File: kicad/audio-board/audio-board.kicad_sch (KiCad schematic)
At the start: 30 parts, among them U1 ADAU1861, U2 ADXL354CEZ, U3 LTC6242, U4 IM72D128VV01, U5 AD2428WBCPZ

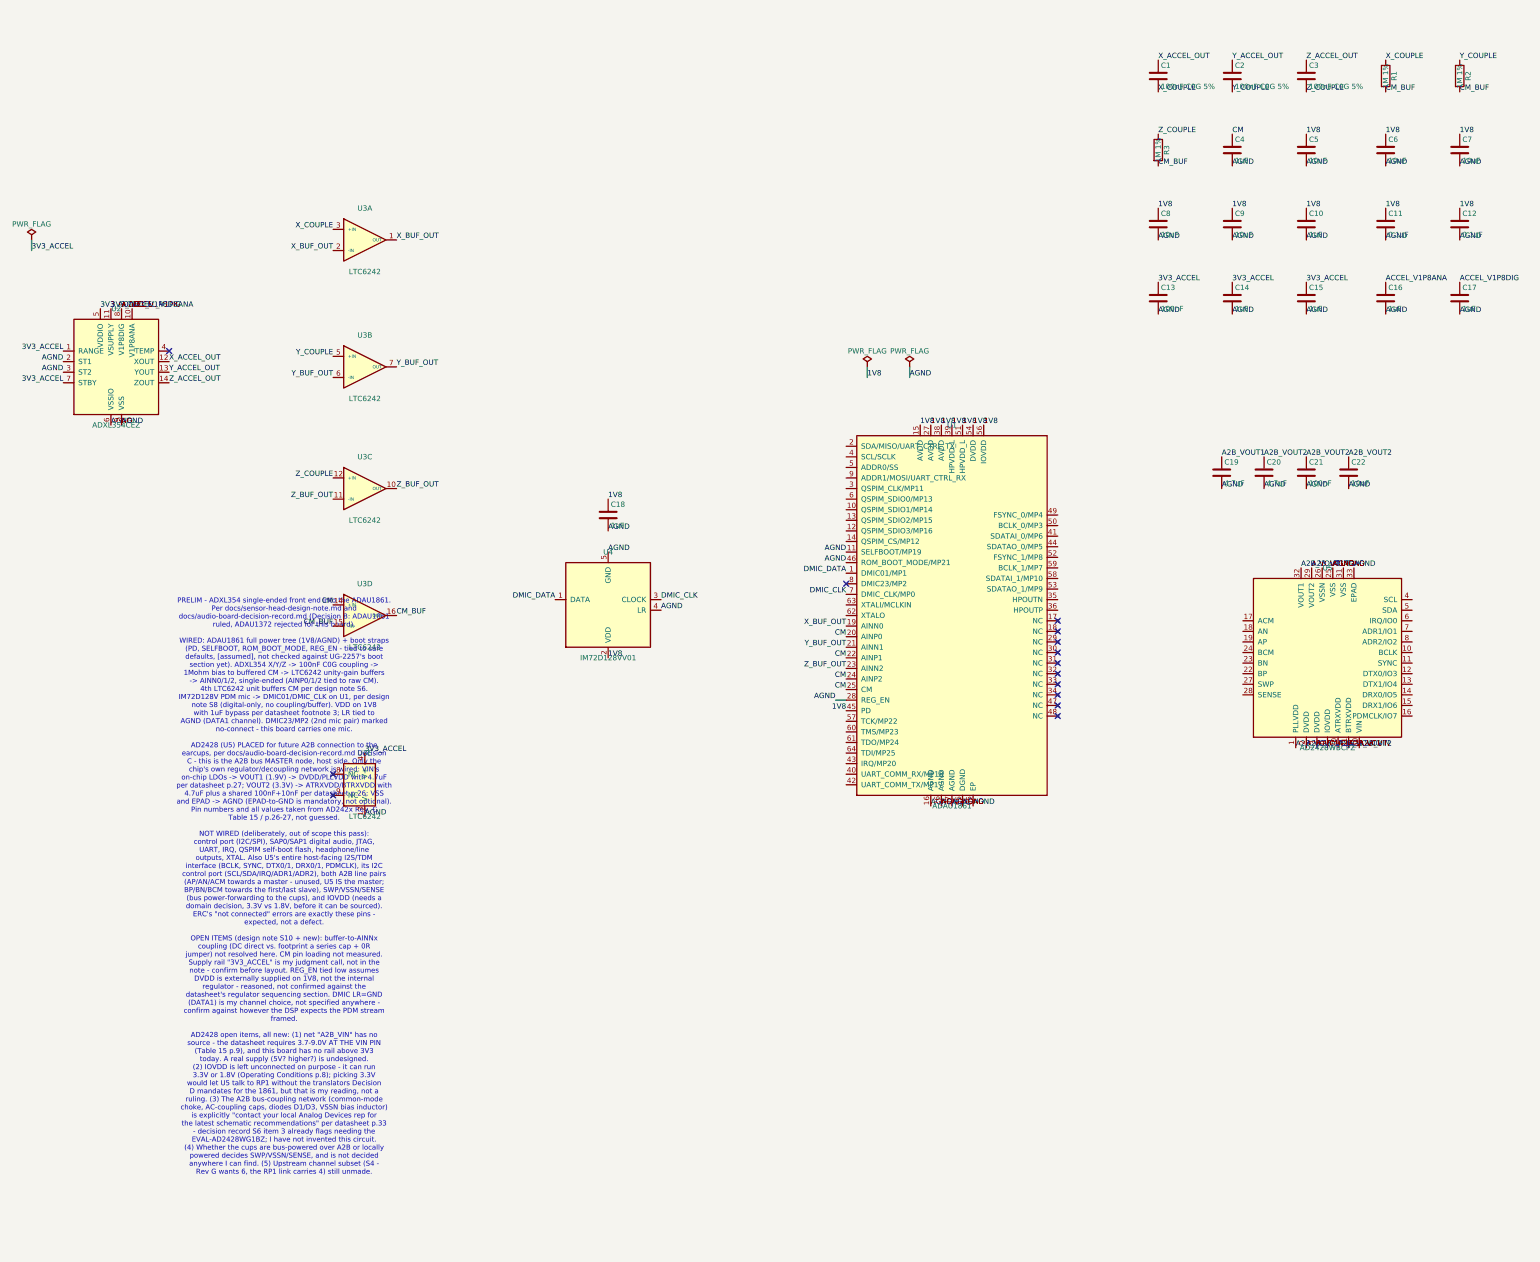
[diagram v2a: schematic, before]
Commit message: [LIMA] cross U1's I2S and I2C to the 3.3V host (CM5/RP1), per docs/audio-board-level-shifter.md
Two SN74LVC8T245 (U6 up, U7 down) carry the five ruled lines - BCLK_0, FSYNC_0, SDATAO_0,
SDATAO_1 up (DIR=1V8), SDATAI_0 down (DIR=AGND) - both parts tied OE=AGND (enabled). Same part on
both per the doc's own "route through the same device type so delays track" rule; U7 is oversized
for its one line on purpose. BCLK_1<-BCLK_0 and FSYNC_1<-FSYNC_0 are wired locally on U1 (no
translator) per the doc's S3.1, keeping SPT0/SPT1 sample-aligned across the two ports carrying the
3-mic array - closes the exact silent-failure mode that section calls out. SDATAI_1 is genuinely
unused (port 1 only outputs) and marked no-connect, not left dangling.

I2C crosses through a PCA9517A (U8), the doc's named part. U1 defaults to I2C mode at power-up
(UG-2257) so no mode strap is needed; ADDR0/ADDR1 tied AGND for address 0x64. Codec-side SCL/SDA
pull-ups are 2.0k to 1V8 - an exact number from the ADAU1861 datasheet's own pin descriptions, not
assumed. Host-side pull-ups (4.7k) are flagged ASSUMED in the schematic's own note: the doc only
says "sized for the bus capacitance" and nothing here states the CM5 cable capacitance.

New "3V3_CM5" rail (assumed CM5-supplied, PWR_FLAG placed accordingly) and a generic 9-pin
connector (J1) stand in for the physical link to the CM5 - deliberately not mapped to real RP1
GPIO numbers, since docs/audio-board-decision-record.md already flags that which CM5 carrier this
is has never been established. New SN74LVC8T245 and PCA9517A symbols (TexasInstruments.kicad_sym,
NXP.kicad_sym) with pinouts fetched directly from ti.com/nxp.com and mirrored into
docs/datasheets/ with fetch-datasheets.sh entries, same convention as the rest of the repo's
gitignored PDFs.

AD2428 (U5) is explicitly untouched by this pass - its own I2S/TDM and I2C to the host stay open
items, called out in the schematic note so nobody assumes U6/U7/U8 carry its traffic too.
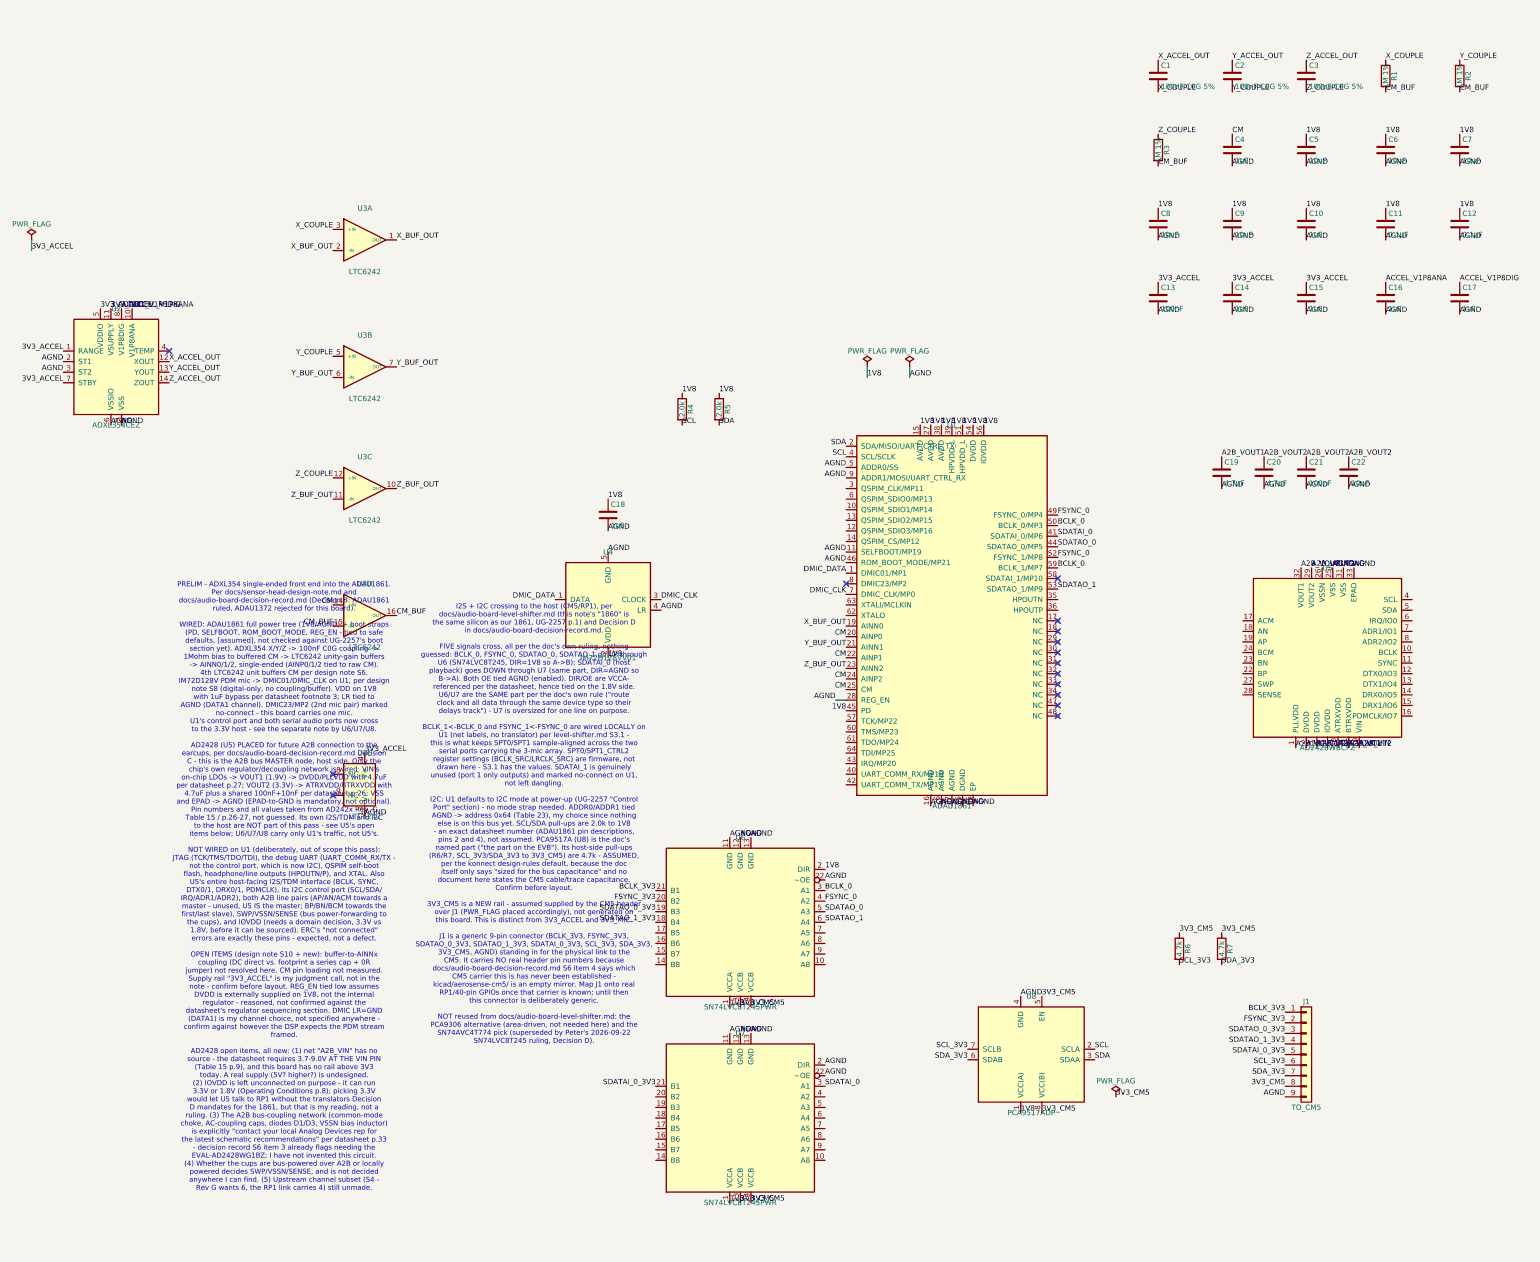
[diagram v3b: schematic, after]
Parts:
- added J1: TO_CM5, symbol Connector_Generic:Conn_01x09
- added R4, R5: 2.0k, symbol Device:R
- added R6, R7: 4.7k, symbol Device:R
- added U6, U7: SN74LVC8T245PWR, symbol TexasInstruments:SN74LVC8T245
- added U8: PCA9517ADP, symbol NXP:PCA9517A
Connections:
- net 1V8: now also R4.1, R5.1, U6.1 (VCCA), U6.2 (DIR), U7.1 (VCCA), U8.1 (VCC(A))
- net AGND: now also U1.5 (ADDR0/SS), U1.9 (ADDR1/MOSI/UART_CTRL_RX), J1.9 (Pin_9), U6.11 (GND), U6.12 (GND), U6.13 (GND), U6.22 (~OE), U7.11 (GND), U7.12 (GND), U7.13 (GND), U7.2 (DIR), U7.22 (~OE), U8.4 (GND)
- net SDA: now reaches U1.2 (SDA/MISO/UART_CTRL_TX)
- net SDA: now also R5.2, U8.3 (SDAA)
- net SCL: now reaches U1.4 (SCL/SCLK)
- net SCL: now also R4.2, U8.2 (SCLA)
- net SDATAI_0: now reaches U1.41 (SDATAI_0/MP6)
- net SDATAI_0: now also U7.3 (A1)
- net SDATAO_0: now reaches U1.44 (SDATAO_0/MP5)
- net SDATAO_0: now also U6.5 (A3)
- net FSYNC_0: now reaches U1.49 (FSYNC_0/MP4)
- net FSYNC_0: now also U1.52 (FSYNC_1/MP8), U6.4 (A2)
- net BCLK_0: now reaches U1.50 (BCLK_0/MP3)
- net BCLK_0: now also U1.59 (BCLK_1/MP7), U6.3 (A1)
- net SDATAO_1: now reaches U1.53 (SDATAO_1/MP9)
- net SDATAO_1: now also U6.6 (A4)
- new net 3V3_CM5: J1.8 (Pin_8), R6.1, R7.1, U6.23 (VCCB), U6.24 (VCCB), U7.23 (VCCB), U7.24 (VCCB), U8.5 (EN), U8.8 (VCC(B))
- new net BCLK_3V3: J1.1 (Pin_1), U6.21 (B1)
- new net FSYNC_3V3: J1.2 (Pin_2), U6.20 (B2)
- new net SCL_3V3: J1.6 (Pin_6), R6.2, U8.7 (SCLB)
- new net SDATAI_0_3V3: J1.5 (Pin_5), U7.21 (B1)
- new net SDATAO_0_3V3: J1.3 (Pin_3), U6.19 (B3)
- new net SDATAO_1_3V3: J1.4 (Pin_4), U6.18 (B4)
- new net SDA_3V3: J1.7 (Pin_7), R7.2, U8.6 (SDAB)
- no-connect marks 14 -> 15
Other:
- note added: "I2S + I2C crossing to the host (CM5/RP1), per docs/audio-board-level-shifter.md (this note's "1860" is the same silicon as our 1861, UG-2257 p.1) and Decision D in docs/audio-board-decision-record.md. FIVE signals cross, all per the doc's own ruling, nothing guessed: BCLK_0, FSYNC_0, SDATAO_0, SDATAO_1 go UP through U6 (SN74LVC8T245, DIR=1V8 so A->B); SDATAI_0 (host playback) goes DOWN through U7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"

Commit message: [LIMA] add VBAT-fed 1.8V/3.3V LDOs (U9/U10) - power source is the aeronode's raw battery, not an external supply
Peter's call: this board's power comes in as VBAT from the aeronode, not as already-regulated rails.
J2 (generic, unmapped - same treatment as J1) stands in for that board-to-board link until the
interconnect is designed. Per kicad/aeronode/doc/ARCHITECTURE.md, VBAT is the raw 2S LiFePO4 pack
net (ahead of aeronode's own charger/buck stage): "the pack never falls below 5.0V" and "the pack
sits at 7.2V" at full charge, so VBAT runs 5.0-7.3V - fetched from that doc, not assumed.

U9 (ADP7118AUJZ-1.8-R7) -> 1V8, U10 (ADP7118AUJZ-3.3-R7) -> 3V3_ACCEL. Deliberately NOT the ADP1715
the EVAL-ADAU1860 uses for this same job (docs/rig-logic-levels.md) - that part is 2.5-5.5V in and
VBAT's 7.3V ceiling is over its max. ADP7118 is the same vendor's wide-input sibling (2.7-20V),
fetched and read directly (analog.com blocked WebFetch again, pulled via an octopart mirror same as
prior ADI parts in this repo). EN tied to VIN (auto-start) and SENSE/ADJ tied to VOUT (fixed-voltage
grade, no divider) per the datasheet's own fixed-output application circuit.

Removed the PWR_FLAG placeholders that used to mark 1V8 and 3V3_ACCEL as "assume externally
supplied" - they have real local sources now. Added one on VBAT instead, since that's the new
board-boundary net. 3V3_CM5 stays untouched by this - it's the host's own rail per the I2S/I2C
note, not something this LDO pair should absorb.

Flagged, not silently wired: AD2428's VIN (3.7-9.0V, still an open item) now has an in-range
candidate in VBAT that didn't exist before this pass. Left for a decision rather than assumed.
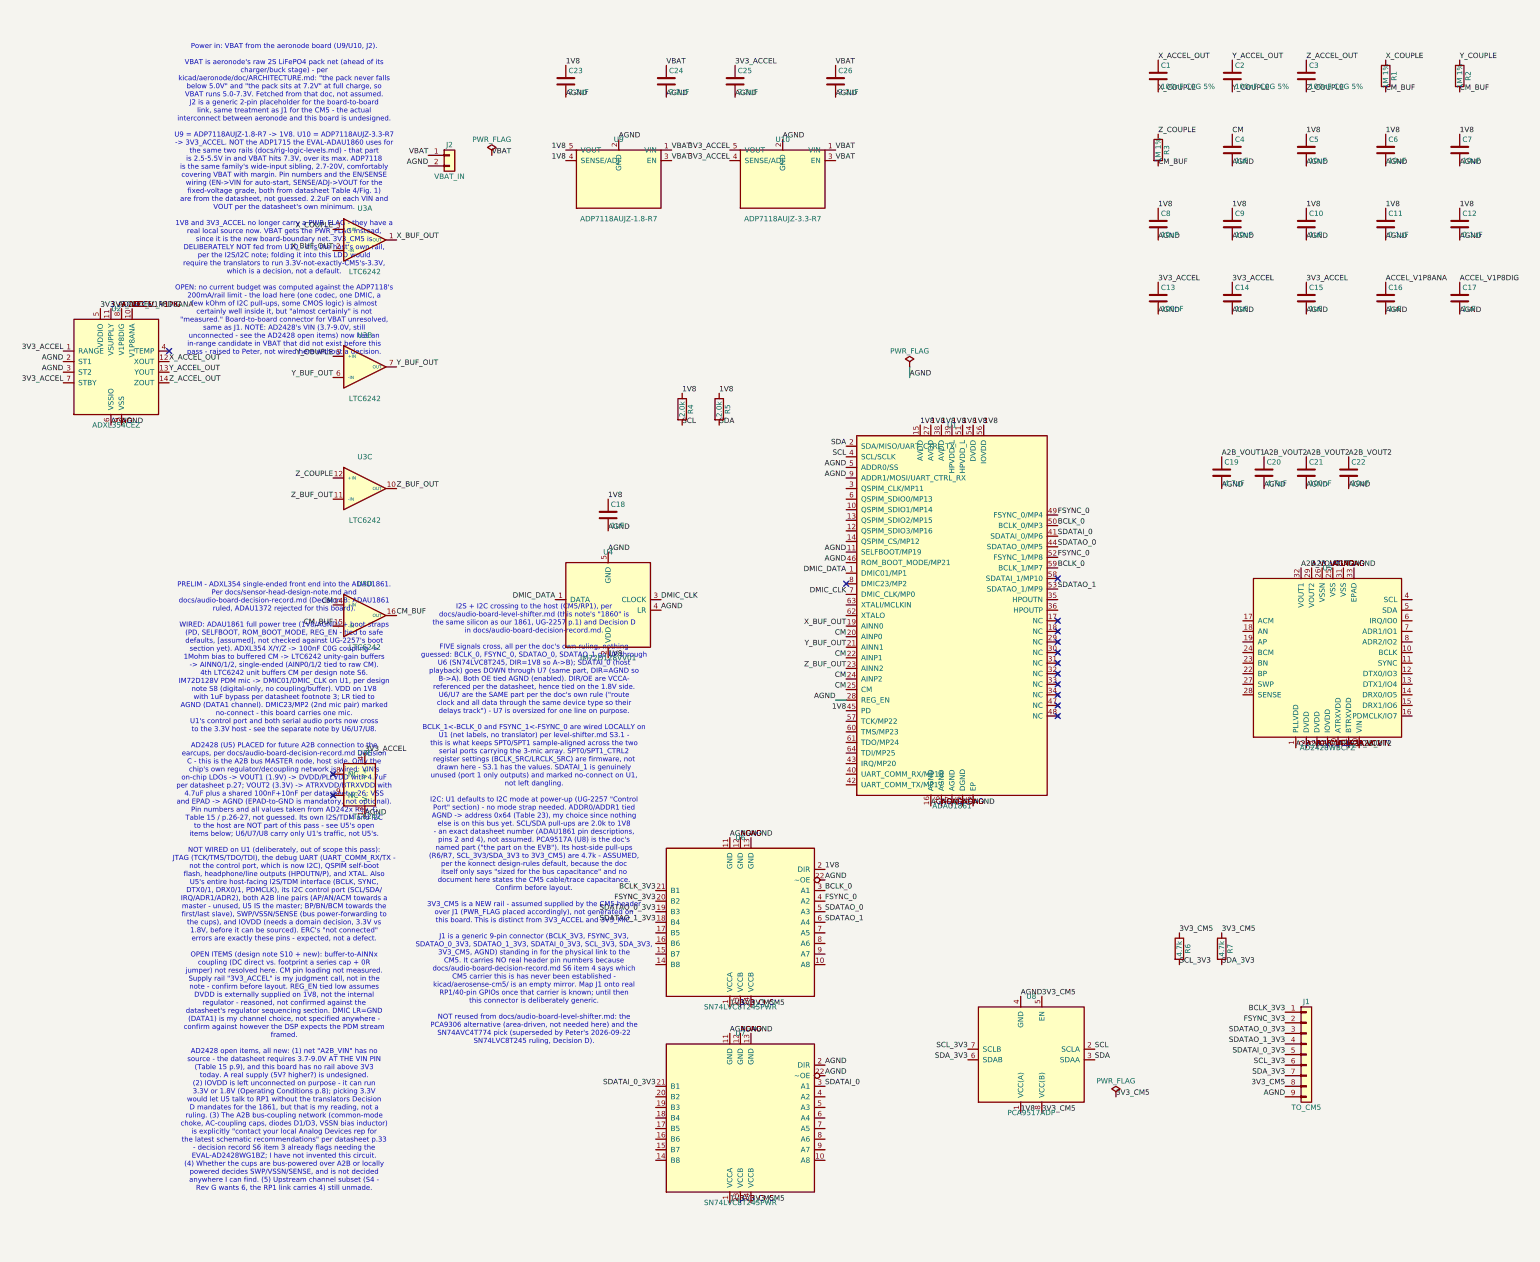
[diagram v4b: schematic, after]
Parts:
- added C23, C24, C25, C26: 2.2uF, symbol Device:C
- added J2: VBAT_IN, symbol Connector_Generic:Conn_01x02
- added U10: ADP7118AUJZ-3.3-R7, symbol AnalogDevices:ADP7118
- added U9: ADP7118AUJZ-1.8-R7, symbol AnalogDevices:ADP7118
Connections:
- net 1V8: now also C23.1, U9.4 (SENSE/ADJ), U9.5 (VOUT)
- net 3V3_ACCEL: now also C25.1, U10.4 (SENSE/ADJ), U10.5 (VOUT)
- net AGND: now also C23.2, C24.2, C25.2, C26.2, J2.2 (Pin_2), U10.2 (GND), U9.2 (GND)
- new net VBAT: C24.1, C26.1, J2.1 (Pin_1), U10.1 (VIN), U10.3 (EN), U9.1 (VIN), U9.3 (EN)
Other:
- note added: "Power in: VBAT from the aeronode board (U9/U10, J2). VBAT is aeronode's raw 2S LiFePO4 pack net (ahead of its charger/buck stage) - per kicad/aeronode/doc/ARCHITECTURE.md: "the pack never falls below 5.0V" and "the pack sits at 7.2V" at full charge, so VBAT runs 5.0-7.3V. Fetched from that doc, not assumed. J2 is a generic 2-pin placeholder for the board-to-board link, same treatment as J1 for th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"
